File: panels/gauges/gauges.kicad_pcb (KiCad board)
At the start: 2 copper layers, 190 x 70 mm, 0 parts

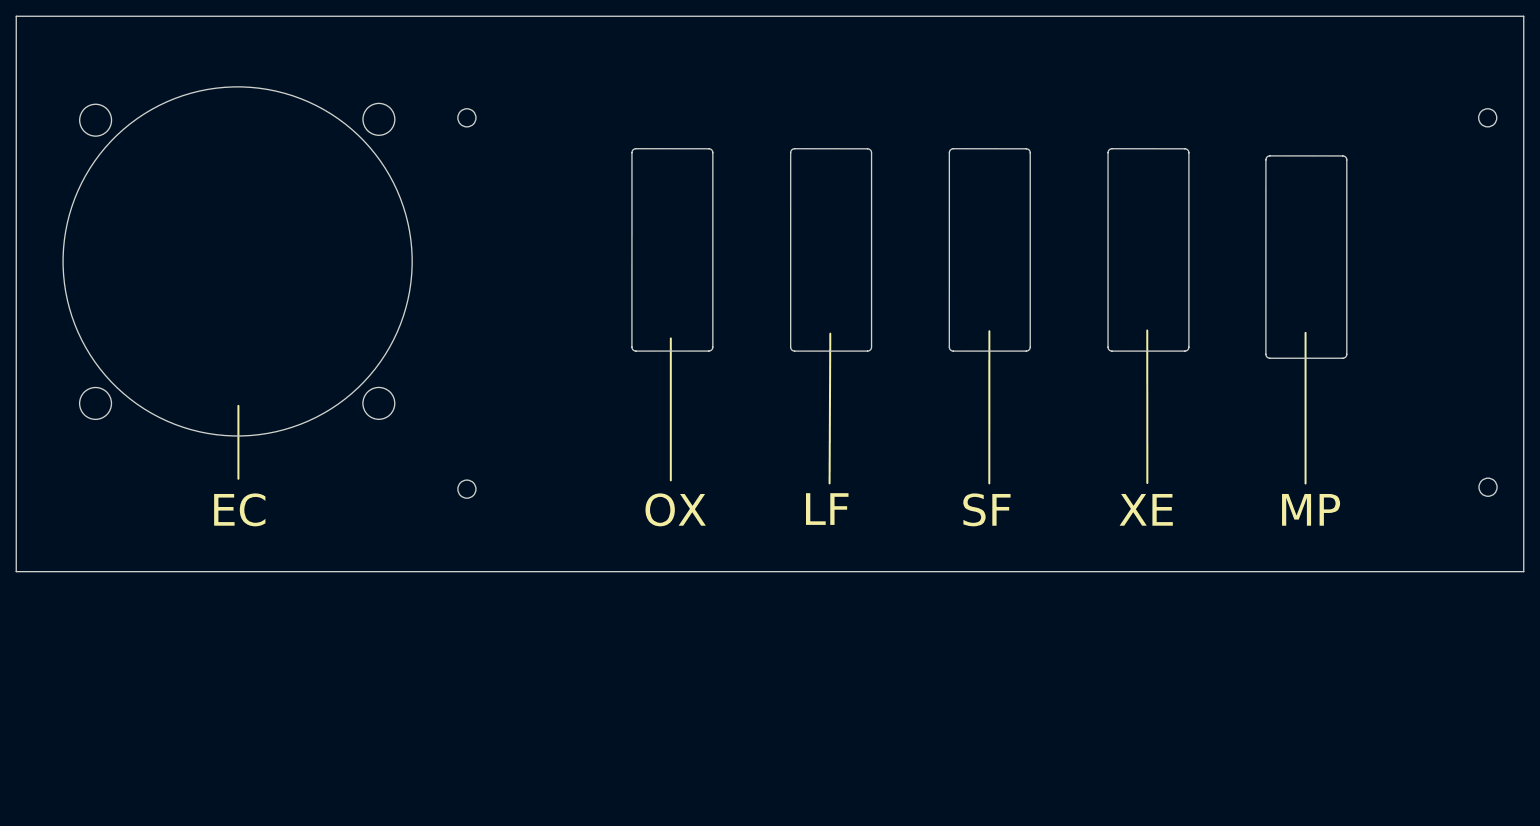
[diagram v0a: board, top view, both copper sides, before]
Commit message: Panels: changed height to 100mm, need to align & anotate 7-seg display
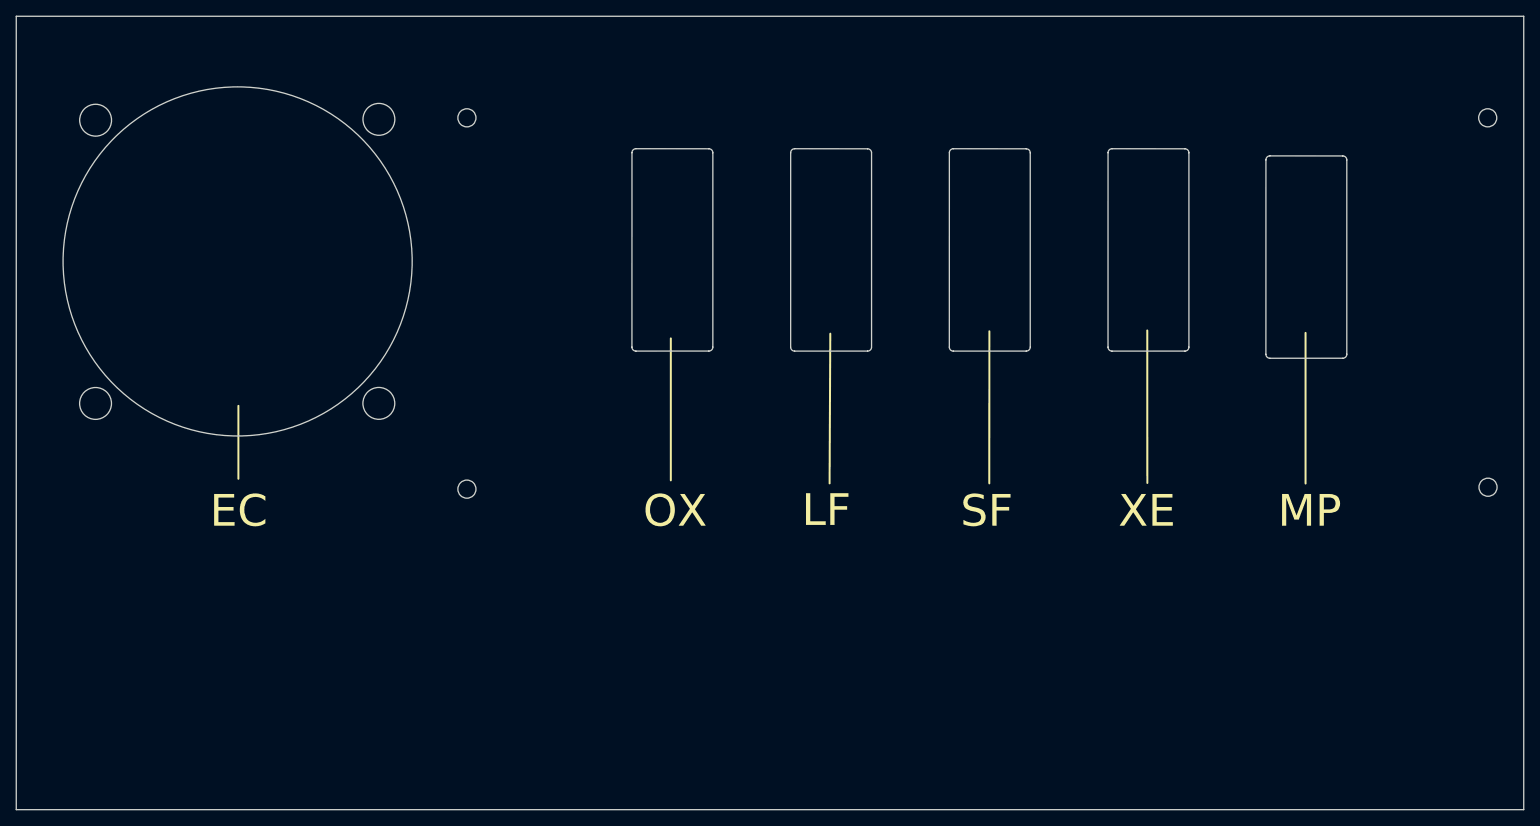
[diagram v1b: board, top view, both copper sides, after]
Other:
- board size 190 x 70 mm -> 190 x 100 mm
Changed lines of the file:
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@@
   (gr_circle (center 27.9 30.9) (end 49.9 30.9)
     (stroke (width 0.1) (type default)) (fill none) (layer "Edge.Cuts"))
-  (gr_rect (start 0 0) (end 190 70)
+  (gr_rect (start 0 0) (end 190 100)
     (stroke (width 0.1) (type default)) (fill none) (layer "Edge.Cuts"))
   (gr_arc (start 117.607106 17.197106) (mid 117.753553 16.843553) (end 118.107106 16.697106)
